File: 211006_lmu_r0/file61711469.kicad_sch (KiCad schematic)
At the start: 4 parts, among them IC1 ADS7038QRTERQ1

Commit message: Updated lmu project with relative library paths and fixed broken symbols
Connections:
- net CSn: now also IC1.11 (~{CS})
- net GND: now also IC1.17 (EP), IC1.9 (GND)
- net Input Filter/Output: now also IC1.15 (AIN0/GPIO0)
- net SCLK: now also IC1.13 (SCLK)
- net SDI: now also IC1.14 (SDI)
- net SDO: now also IC1.12 (SDO)
- net VREG: now also IC1.10 (DVDD)
- net sheet616CF5C4/Output: now also IC1.16 (AIN1/GPIO1)
- net sheet616CF701/Output: now also IC1.1 (AIN2/GPIO2)
- net sheet616CF702/Output: now also IC1.2 (AIN3/GPIO3)
- net sheet616D00FD/Output: now also IC1.3 (AIN4/GPIO4)
- net sheet616D00FE/Output: now also IC1.4 (AIN5/GPIO5)
- net sheet616D00FF/Output: now also IC1.5 (AIN6/GPIO6)
- net sheet616D0100/Output: now also IC1.6 (AIN7/GPIO7)
- net at C14.1: now also IC1.7 (AVDD)
- net at C15.1: now also IC1.8 (DECAP)
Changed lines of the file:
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@@
       (effects (font (size 1.27 1.27)) hide)
     )
+    (pin "1")
+    (pin "10")
+    (pin "11")
+    (pin "12")
+    (pin "13")
+    (pin "14")
+    (pin "15")
+    (pin "16")
+    (pin "17")
+    (pin "2")
+    (pin "3")
+    (pin "4")
+    (pin "5")
+    (pin "6")
+    (pin "7")
+    (pin "8")
+    (pin "9")
   )
   (symbol (lib_id "Device:C") (at 207.01 91.44 0) (unit 1)

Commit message: Updated some components to make sourcing easier
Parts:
- C14, C15, C16: Manufacturer (none) -> -; Part Number (none) -> -
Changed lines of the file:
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@@
+      (effects (font (size 1.27 1.27)) hide)
+    )
+    (property "Part Number" "-" (id 4) (at 207.01 91.44 0)
+      (effects (font (size 1.27 1.27)) hide)
+    )
+    (property "Manufacturer" "-" (id 5) (at 207.01 91.44 0)
       (effects (font (size 1.27 1.27)) hide)
     )
@@
       (effects (font (size 1.27 1.27)) hide)
     )
+    (property "Part Number" "-" (id 4) (at 214.63 91.44 0)
+      (effects (font (size 1.27 1.27)) hide)
+    )
+    (property "Manufacturer" "-" (id 5) (at 214.63 91.44 0)
+      (effects (font (size 1.27 1.27)) hide)
+    )
     (pin "1")
     (pin "2")
@@
       (effects (font (size 1.27 1.27)) hide)
     )
+    (property "Part Number" "-" (id 4) (at 222.25 91.44 0)
+      (effects (font (size 1.27 1.27)) hide)
+    )
+    (property "Manufacturer" "-" (id 5) (at 222.25 91.44 0)
+      (effects (font (size 1.27 1.27)) hide)
+    )

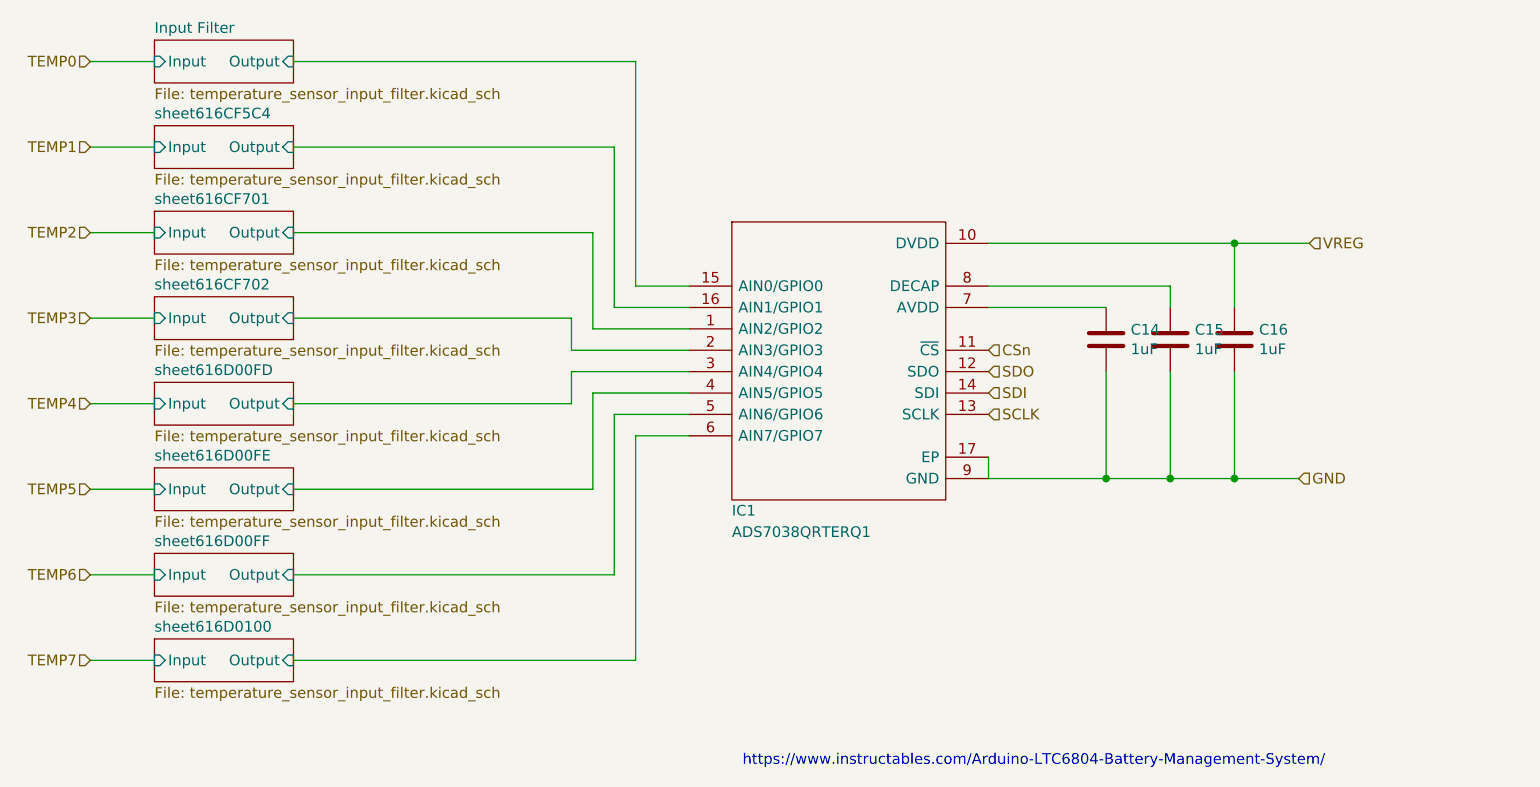
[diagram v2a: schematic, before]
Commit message: fixed footprints for headers, started planning out zones
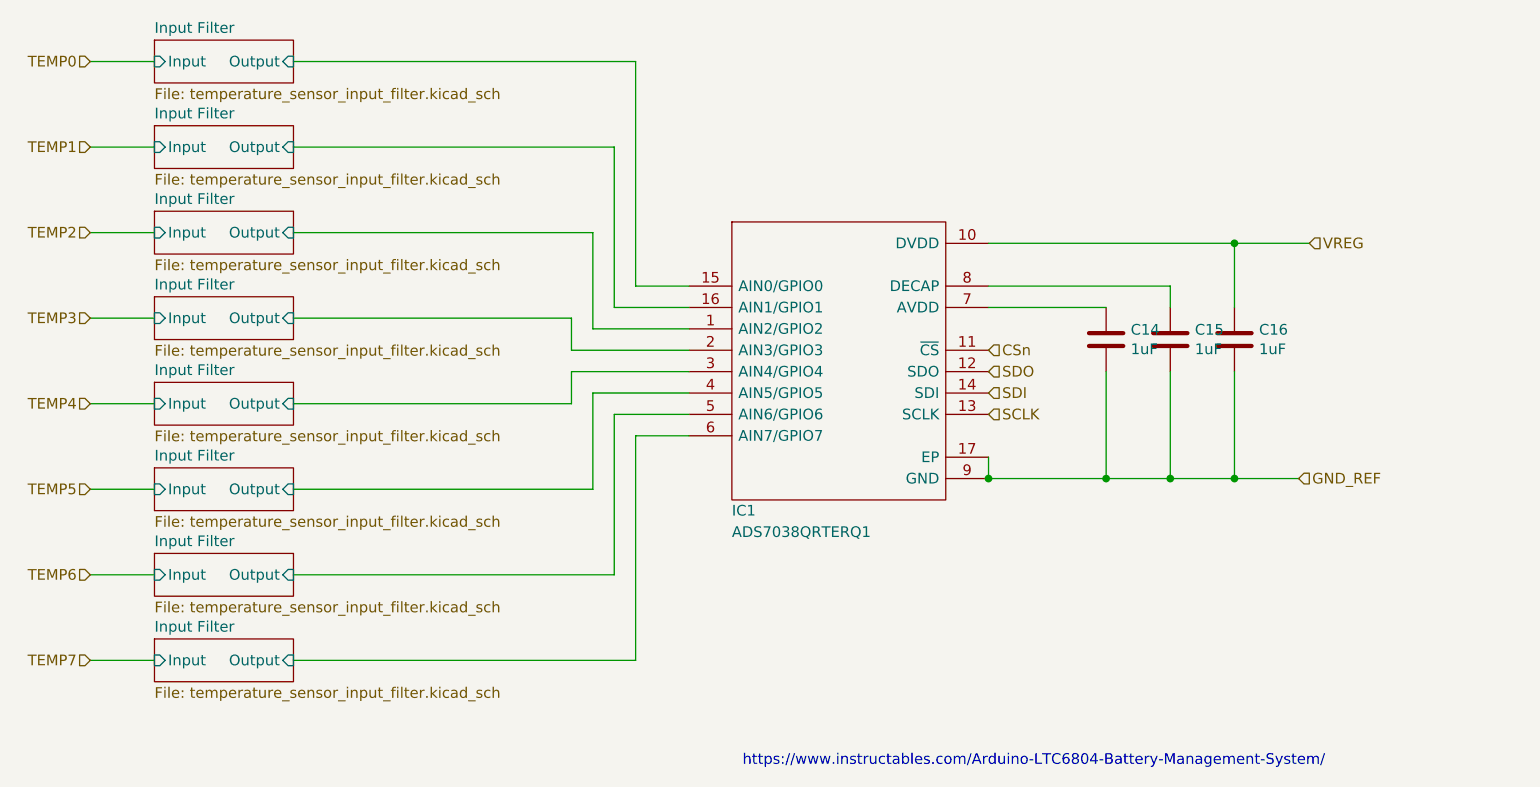
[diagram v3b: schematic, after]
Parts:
- IC1: footprint QFN50P300X300X80-17N-D -> Package_DFN_QFN:WQFN-16-1EP_3x3mm_P0.5mm_EP1.6x1.6mm
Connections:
- net sheet616D0100/Output is gone; now on net Input Filter/Output: IC1.6 (AIN7/GPIO7)
- net Input Filter/Output: no longer IC1.15 (AIN0/GPIO0)
- net GND renamed GND_REF
- net sheet616CF5C4/Output renamed Input Filter/Output
- net sheet616CF701/Output renamed Input Filter/Output
- net sheet616CF702/Output renamed Input Filter/Output
- net sheet616D00FD/Output renamed Input Filter/Output
- net sheet616D00FE/Output renamed Input Filter/Output
- net sheet616D00FF/Output renamed Input Filter/Output
- new net Input Filter/Output: IC1.15 (AIN0/GPIO0)
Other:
- removed sheet sheet616CF5C4
- removed sheet sheet616CF701
- removed sheet sheet616CF702
- removed sheet sheet616D00FD
- removed sheet sheet616D00FE
- removed sheet sheet616D00FF
- removed sheet sheet616D0100
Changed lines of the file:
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@@
   (junction (at 222.25 107.95) (diameter 0) (color 0 0 0 0)
   )
+  (junction (at 214.63 107.95) (diameter 0) (color 0 0 0 0)
+  )
+  (junction (at 193.04 107.95) (diameter 0) (color 0 0 0 0)
+  )
+  (junction (at 222.25 80.01) (diameter 0) (color 0 0 0 0)
+  )
   (junction (at 207.01 107.95) (diameter 0) (color 0 0 0 0)
   )
-  (junction (at 214.63 107.95) (diameter 0) (color 0 0 0 0)
-  )
-  (junction (at 222.25 80.01) (diameter 0) (color 0 0 0 0)
-  )
   (wire (pts (xy 222.25 95.25) (xy 222.25 107.95))
     (stroke (width 0) (type default) (color 0 0 0 0))
@@
     (stroke (width 0) (type default) (color 0 0 0 0))
   )
+  (wire (pts (xy 193.04 105.41) (xy 193.04 107.95))
+    (stroke (width 0) (type default) (color 0 0 0 0))
+  )
   (wire (pts (xy 207.01 95.25) (xy 207.01 107.95))
     (stroke (width 0) (type default) (color 0 0 0 0))
@@
     (stroke (width 0) (type default) (color 0 0 0 0))
   )
-  (wire (pts (xy 193.04 105.41) (xy 193.04 107.95))
+  (wire (pts (xy 193.04 107.95) (xy 207.01 107.95))
     (stroke (width 0) (type default) (color 0 0 0 0))
   )
@@
   )
   (wire (pts (xy 148.59 119.38) (xy 148.59 100.33))
-    (stroke (width 0) (type default) (color 0 0 0 0))
-  )
-  (wire (pts (xy 193.04 107.95) (xy 207.01 107.95))
     (stroke (width 0) (type default) (color 0 0 0 0))
   )
@@
     (effects (font (size 1.27 1.27)) (justify right))
   )
-  (hierarchical_label "GND" (shape input) (at 229.87 107.95 0)
+  (hierarchical_label "GND_REF" (shape input) (at 229.87 107.95 0)
     (effects (font (size 1.27 1.27)) (justify left))
   )
@@
       (effects (font (size 1.27 1.27)) (justify left))
     )
-    (property "Footprint" "QFN50P300X300X80-17N-D" (id 2) (at 189.23 72.39 0)
+    (property "Footprint" "Package_DFN_QFN:WQFN-16-1EP_3x3mm_P0.5mm_EP1.6x1.6mm" (id 2) (at 189.23 72.39 0)
       (effects (font (size 1.27 1.27)) (justify left) hide)
     )
@@
     (stroke (width 0) (type solid) (color 0 0 0 0))
     (fill (color 0 0 0 0.0000))
-    (property "Sheet name" "sheet616CF5C4" (id 0) (at 93.98 65.3284 0)
+    (property "Sheet name" "Input Filter" (id 0) (at 93.98 65.3284 0)
       (effects (font (size 1.27 1.27)) (justify left bottom))
     )
@@
     (stroke (width 0) (type solid) (color 0 0 0 0))
     (fill (color 0 0 0 0.0000))
-    (property "Sheet name" "sheet616CF701" (id 0) (at 93.98 75.4884 0)
+    (property "Sheet name" "Input Filter" (id 0) (at 93.98 75.4884 0)
       (effects (font (size 1.27 1.27)) (justify left bottom))
     )
@@
     (stroke (width 0) (type solid) (color 0 0 0 0))
     (fill (color 0 0 0 0.0000))
-    (property "Sheet name" "sheet616CF702" (id 0) (at 93.98 85.6484 0)
+    (property "Sheet name" "Input Filter" (id 0) (at 93.98 85.6484 0)
       (effects (font (size 1.27 1.27)) (justify left bottom))
     )
@@
     (stroke (width 0) (type solid) (color 0 0 0 0))
     (fill (color 0 0 0 0.0000))
-    (property "Sheet name" "sheet616D00FD" (id 0) (at 93.98 95.8084 0)
+    (property "Sheet name" "Input Filter" (id 0) (at 93.98 95.8084 0)
       (effects (font (size 1.27 1.27)) (justify left bottom))
     )
@@
     (stroke (width 0) (type solid) (color 0 0 0 0))
     (fill (color 0 0 0 0.0000))
-    (property "Sheet name" "sheet616D00FE" (id 0) (at 93.98 105.9684 0)
+    (property "Sheet name" "Input Filter" (id 0) (at 93.98 105.9684 0)
       (effects (font (size 1.27 1.27)) (justify left bottom))
     )
@@
     (stroke (width 0) (type solid) (color 0 0 0 0))
     (fill (color 0 0 0 0.0000))
-    (property "Sheet name" "sheet616D00FF" (id 0) (at 93.98 116.1284 0)
+    (property "Sheet name" "Input Filter" (id 0) (at 93.98 116.1284 0)
       (effects (font (size 1.27 1.27)) (justify left bottom))
     )
@@
     (stroke (width 0) (type solid) (color 0 0 0 0))
     (fill (color 0 0 0 0.0000))
-    (property "Sheet name" "sheet616D0100" (id 0) (at 93.98 126.2884 0)
-      (effects (font (size 1.27 1.27)) (justify left bottom))
-    )
+    (property "Sheet name" "Input Filter" (id 0) (at 93.98 126.2884 0)
+      (effects (font (size 1.27 1.27)) (justify left bottom))
+    )

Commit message: Lots of routing and placing, according to planned layout
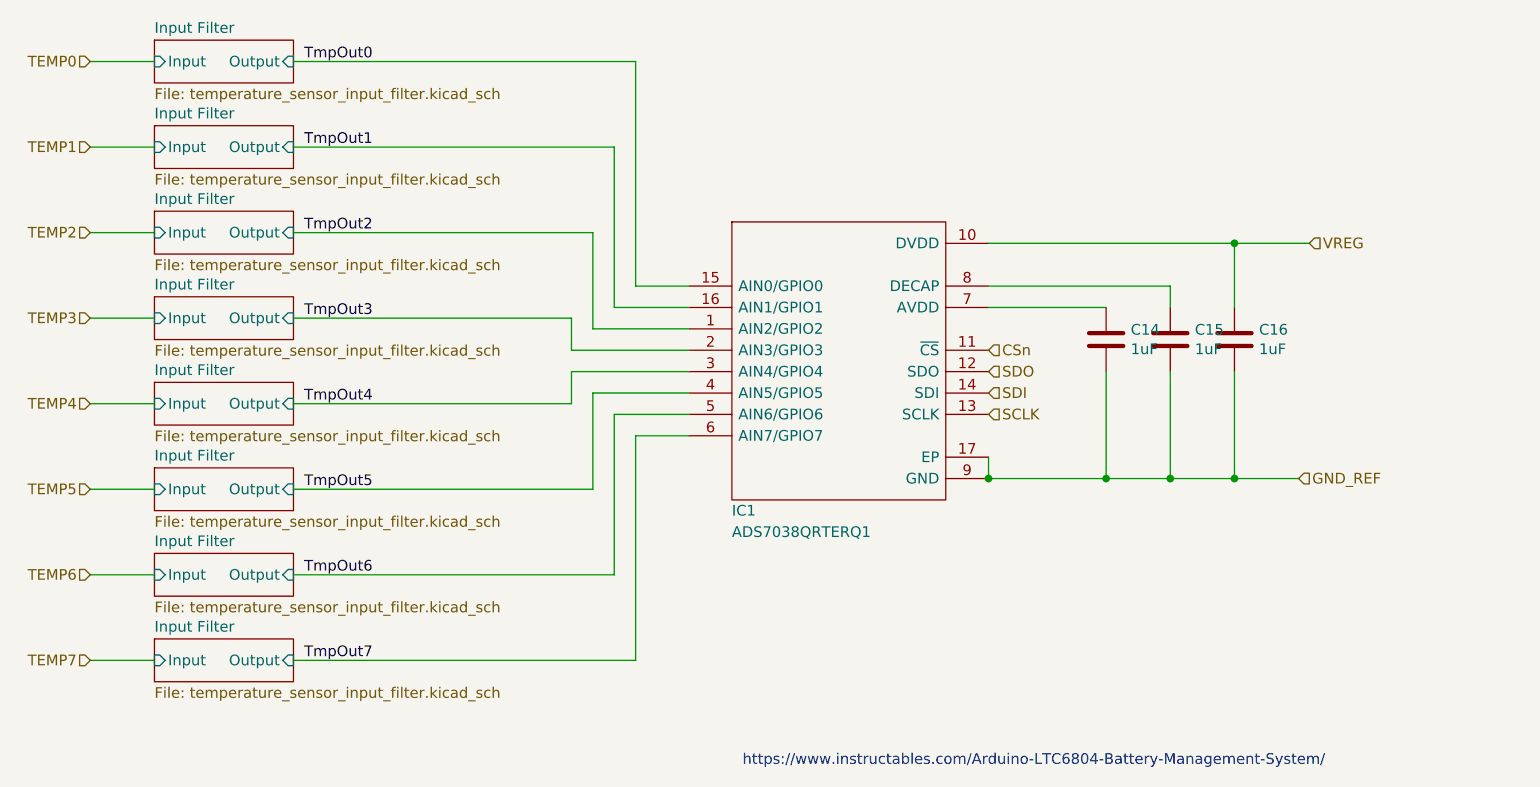
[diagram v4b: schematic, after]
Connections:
- net Input Filter/Output renamed TmpOut2
- net Input Filter/Output renamed TmpOut0
- net Input Filter/Output renamed TmpOut1
- net Input Filter/Output renamed TmpOut3
- net Input Filter/Output renamed TmpOut4
- net Input Filter/Output renamed TmpOut5
- net Input Filter/Output renamed TmpOut6
- net Input Filter/Output renamed TmpOut7
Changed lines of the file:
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@@
+    (effects (font (size 1.27 1.27)) (justify left bottom))
+  )
+  (label "TmpOut7" (at 111.76 129.54 0)
+    (effects (font (size 1.27 1.27)) (justify left bottom))
+  )
+  (label "TmpOut4" (at 111.76 99.06 0)
+    (effects (font (size 1.27 1.27)) (justify left bottom))
+  )
+  (label "TmpOut0" (at 111.76 58.42 0)
+    (effects (font (size 1.27 1.27)) (justify left bottom))
+  )
+  (label "TmpOut5" (at 111.76 109.22 0)
+    (effects (font (size 1.27 1.27)) (justify left bottom))
+  )
+  (label "TmpOut3" (at 111.76 88.9 0)
+    (effects (font (size 1.27 1.27)) (justify left bottom))
+  )
+  (label "TmpOut2" (at 111.76 78.74 0)
+    (effects (font (size 1.27 1.27)) (justify left bottom))
+  )
+  (label "TmpOut6" (at 111.76 119.38 0)
+    (effects (font (size 1.27 1.27)) (justify left bottom))
+  )
+  (label "TmpOut1" (at 111.76 68.58 0)
     (effects (font (size 1.27 1.27)) (justify left bottom))
   )

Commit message: merge PCB
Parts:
- IC1: value ADS7038QRTERQ1 -> ADS7028QRTERQ1; Mouser Price/Stock https://www.mouser.co.uk/ProductDetail/Texas-Instruments/AD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 -> https://au.mouser.com/ProductDetail/Texas-Instruments/ADS70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; Mouser URL NOT AVAILABLE! -> (none); Part Number ADS7038QRTERQ1 -> ADS7028IRTER
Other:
- note added: "switched for 7028, same footprint"
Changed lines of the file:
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@@
+    (effects (font (size 1.27 1.27)) (justify left bottom))
+  )
+  (text "switched for 7028, same footprint" (at 157.48 119.38 0)
     (effects (font (size 1.27 1.27)) (justify left bottom))
   )
@@
       (effects (font (size 1.27 1.27)) (justify left))
     )
-    (property "Value" "ADS7038QRTERQ1" (id 1) (at 162.56 114.3 0)
+    (property "Value" "ADS7028QRTERQ1" (id 1) (at 162.56 114.3 0)
       (effects (font (size 1.27 1.27)) (justify left))
     )
@@
       (effects (font (size 1.27 1.27)) (justify left) hide)
     )
-    (property "Datasheet" "https://www.ti.com/lit/ds/symlink/ads7038-q1.pdf?ts=1609502413909&ref_url=https%253A%252F%252Fwww.ti.com%252Fstore%252Fti%252Fen%252Fp%252Fproduct%252F%253Fp%253DADS7038QRTERQ1%2526keyMatch%253DADS7038QRTERQ1%2526tisearch%253DSearch-EN-everything%2526usec" (id 3) (at 189.23 74.93 0)
+    (property "Datasheet" "https://www.ti.com/lit/ds/symlink/ads7028.pdf?ts=1650347374272&ref_url=https%253A%252F%252Fau.mouser.com%252F" (id 3) (at 189.23 74.93 0)
       (effects (font (size 1.27 1.27)) (justify left) hide)
     )
-    (property "Description" "ADS7038 Q1 Small 8 Channel 12 Bit ADC With SPI Interface and CRC" (id 4) (at 189.23 77.47 0)
+    (property "Description" "ADS7028 Q1 Small 8 Channel 12 Bit ADC With SPI Interface and CRC" (id 4) (at 189.23 77.47 0)
       (effects (font (size 1.27 1.27)) (justify left) hide)
     )
@@
       (effects (font (size 1.27 1.27)) (justify left) hide)
     )
-    (property "Mouser Price/Stock" "https://www.mouser.co.uk/ProductDetail/Texas-Instruments/ADS7038QRTERQ1?qs=81r%252BiQLm7BTk46c4kXEtDw%3D%3D" (id 7) (at 189.23 85.09 0)
+    (property "Mouser Price/Stock" "https://au.mouser.com/ProductDetail/Texas-Instruments/ADS7028IRTER?qs=%252B6g0mu59x7L0mzHBJBWvJw%3D%3D" (id 7) (at 189.23 85.09 0)
       (effects (font (size 1.27 1.27)) (justify left) hide)
     )
@@
       (effects (font (size 1.27 1.27)) hide)
     )
-    (property "Part Number" "ADS7038QRTERQ1" (id 11) (at 157.48 90.17 0)
+    (property "Part Number" "ADS7028IRTER" (id 11) (at 157.48 90.17 0)
       (effects (font (size 1.27 1.27)) hide)
     )
-    (property "Mouser URL" "NOT AVAILABLE!" (id 12) (at 157.48 90.17 0)
+    (property "Mouser URL" "" (id 12) (at 157.48 90.17 0)
       (effects (font (size 1.27 1.27)) hide)
     )
